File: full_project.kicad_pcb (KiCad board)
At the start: 2 copper layers, 88.5 x 86.1 mm, 46 parts, among them J1 Conn_01x16, J10 Screw_Terminal_01x02, J12 V_OFFSET, J14 Conn_01x02, J2 Raspberry_Pi_2_3, J3 Conn_01x08, J4 Screw_Terminal_01x04_titrator, J5 RF_Shield_Two_Pieces, J6 BNC_Jack, J7 SJ-43515TS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

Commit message: cache and stuff
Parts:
- removed the J5 at (148.2, 81.7) (x2)
- added J5 (x2): RF_Shield_Two_Pieces, Titrator_Footprints:44-CBSA-1.0X1.5X0.4, F.Cu at (148.2, 81.7)

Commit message: Please just push
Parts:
- removed the J5 at (148.2, 81.7) (x2)
- added J5 (x2): RF_Shield_Two_Pieces, Titrator_Footprints:44-CBSA-1.0X1.5X0.4, F.Cu at (148.2, 81.7)

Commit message: I don't want github to throw a fit
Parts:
- removed the J5 at (148.2, 81.7) (x2)
- added J5 (x2): RF_Shield_Two_Pieces, Titrator_Footprints:44-CBSA-1.0X1.5X0.4, F.Cu at (148.2, 81.7)
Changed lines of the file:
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@@
-(kicad_pcb (version 20171130) (host pcbnew "(5.1.9)-1")
+(kicad_pcb (version 20171130) (host pcbnew "(5.1.5)-3")
   (general
     (thickness 1.6)
@@
     (38 B.Mask user)
     (39 F.Mask user)
-    (40 Dwgs.User user hide)
+    (40 Dwgs.User user)
     (41 Cmts.User user hide)
     (42 Eco1.User user hide)
@@
       (scale (xyz 1 1 1))
       (rotate (xyz -90 0 0))
+    )
+    (model ${KIPRJMOD}/imported_3d/BNC-Connector-Straight.step
+      (offset (xyz 0 37 6.5))
+      (scale (xyz 1 1 1))
+      (rotate (xyz -90 0 0))

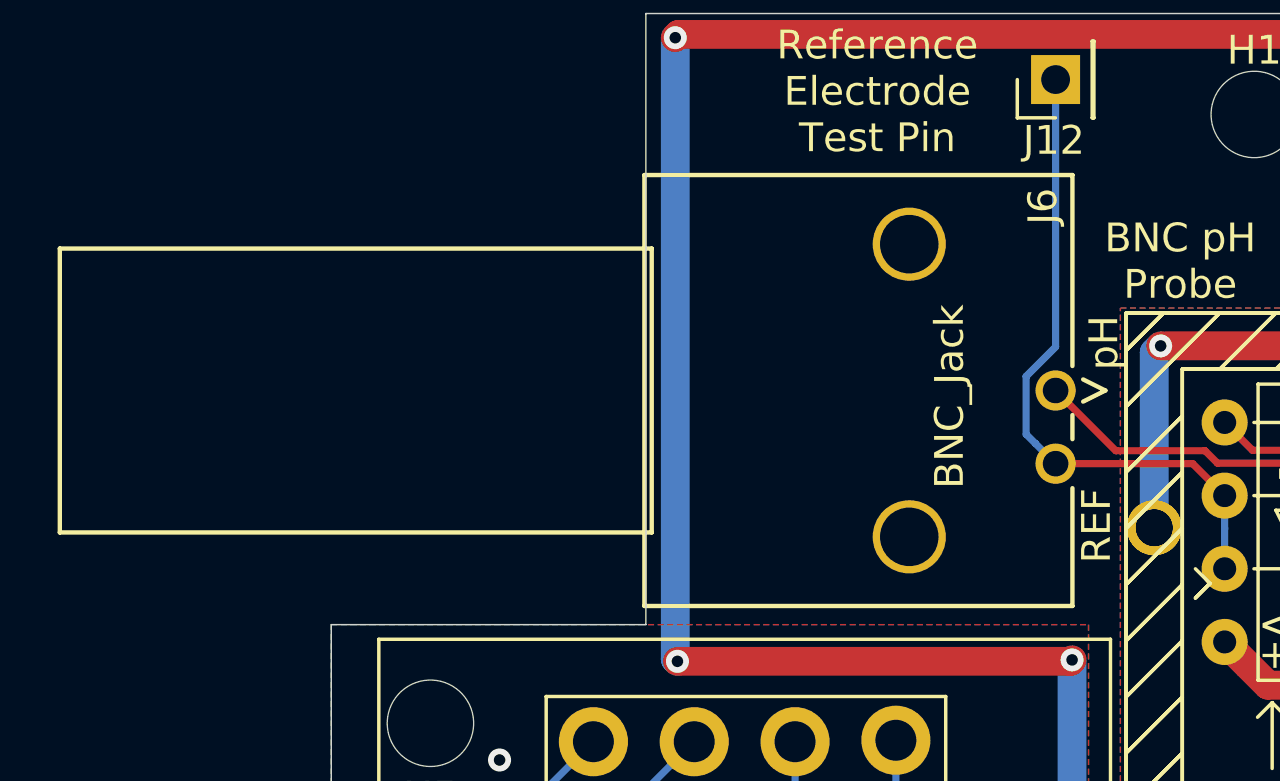
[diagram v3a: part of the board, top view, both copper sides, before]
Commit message: Rev 3 schematic update, expanded footprint library for custom models
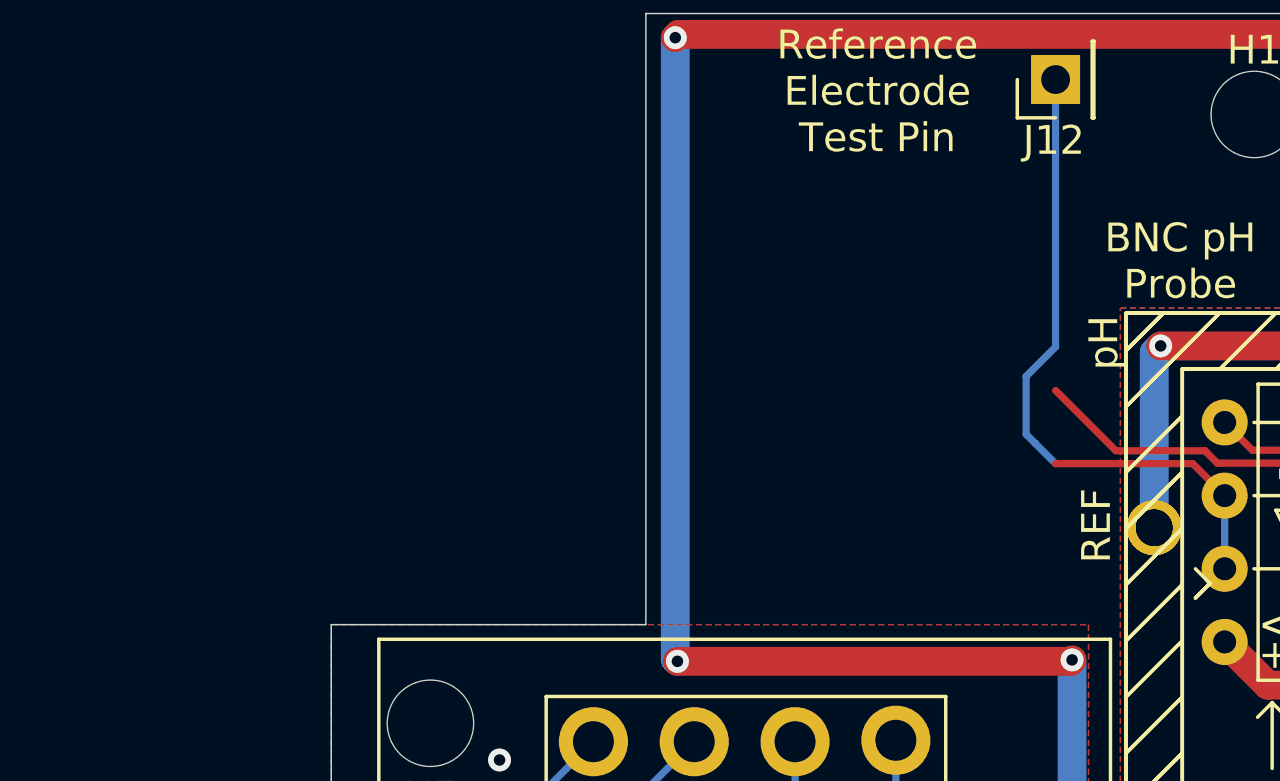
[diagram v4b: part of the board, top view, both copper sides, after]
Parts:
- removed the J5 at (148.2, 81.7) (x2)
- removed J6: BNC_Jack, Titrator_Footprints:BNC_Jack
- added J5 (x2): RF_Shield_Two_Pieces, Titrator_Footprints:44-CBSA-1.0X1.5X0.4, F.Cu at (148.2, 81.7)
- H2, H4: footprint MountingHole:MountingHole_3mm -> Titrator_Footprints:MountingHole_3mm
